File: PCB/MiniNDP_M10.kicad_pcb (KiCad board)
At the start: 2 copper layers, 72 x 26 mm, 22 parts, among them J1 Conn_02x20_Odd_Even, U1 AS6C8008_TSOPII, U2 HC238, U3 HC4040, U4 ABT841

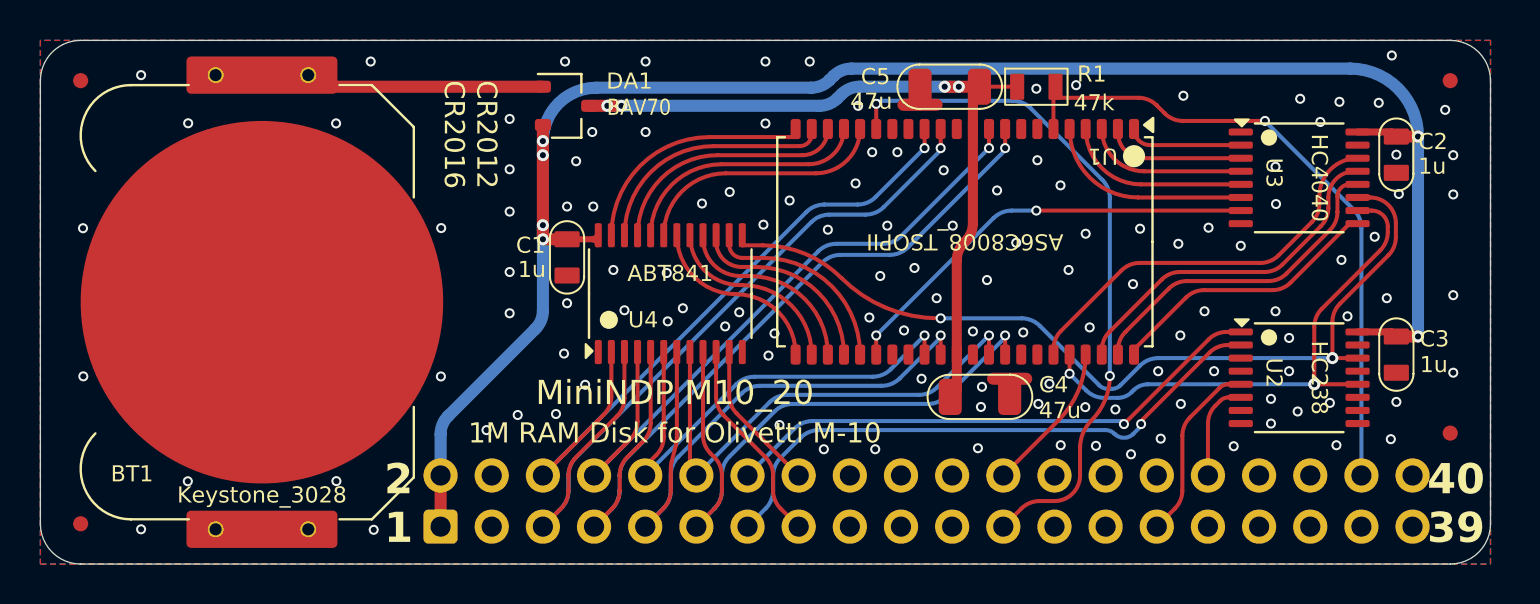
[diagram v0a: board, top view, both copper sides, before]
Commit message: M10 better layout, put old M10 versions in attic
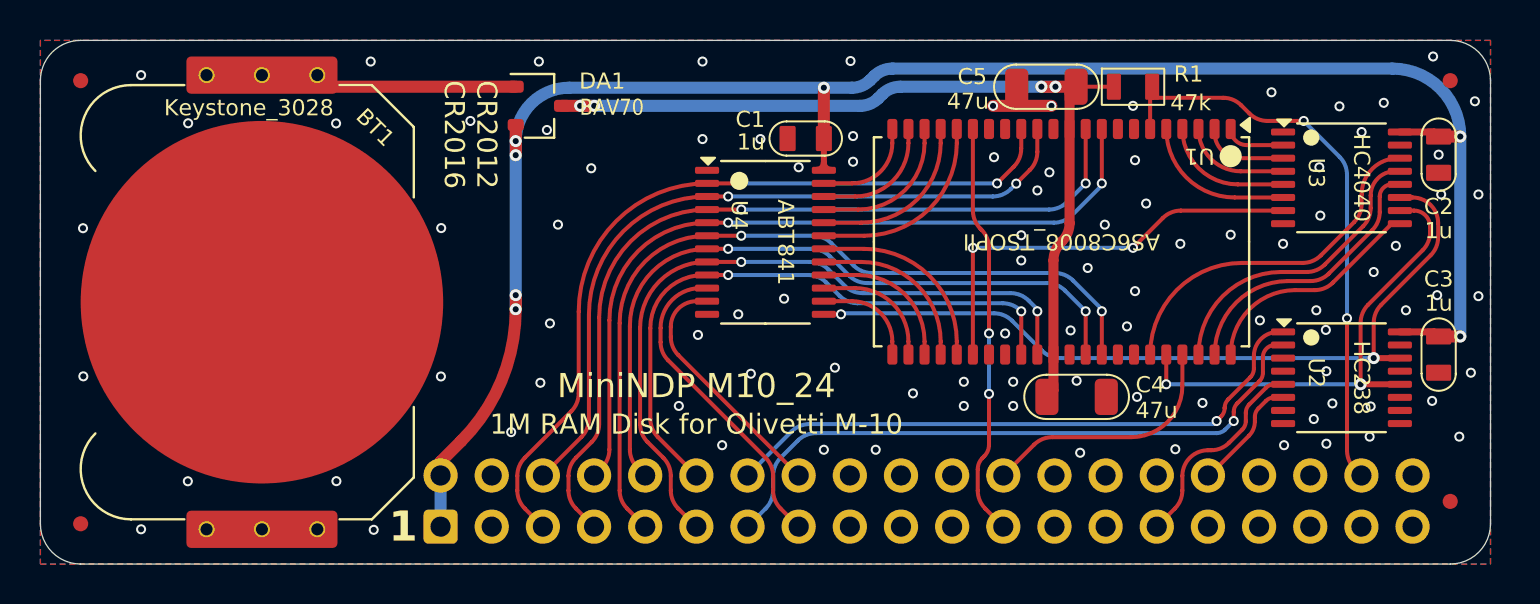
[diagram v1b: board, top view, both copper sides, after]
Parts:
- removed the REF** at (116.0, 116.3)
- removed the REF** at (120.7, 93.8)
- removed the REF** at (116.0, 93.8)
- removed the REF** at (120.7, 116.3)
- added REF**: pth_nail, 000_LOCAL:pth_nail, F.Cu at (118.3, 93.8)
- added REF**: pth_nail, 000_LOCAL:pth_nail, F.Cu at (121.1, 116.3)
- added REF**: pth_nail, 000_LOCAL:pth_nail, F.Cu at (118.3, 116.3)
- added REF**: pth_nail, 000_LOCAL:pth_nail, F.Cu at (115.6, 116.3)
- added REF**: pth_nail, 000_LOCAL:pth_nail, F.Cu at (121.1, 93.8)
- added REF**: pth_nail, 000_LOCAL:pth_nail, F.Cu at (115.6, 93.8)
- moved C1 13.2 mm to (145.3, 96.9), turned to 180 degrees
- moved U4 5.37 mm to (143.3, 102.0), turned to 0 degrees
- moved C4 4.80 mm to (158.8, 109.7)
- moved C5 4.80 mm to (157.3, 94.3)
- moved U1 4.80 mm to (158.1, 102.0)
- moved R1 4.80 mm to (161.6, 94.3)
- moved F3 3.39 mm to (177.3, 114.9)
- moved C2 2.10 mm to (176.8, 97.7)
- moved C3 2.10 mm to (176.8, 107.6)
- moved U2 2.10 mm to (172.0, 108.8)
- moved U3 2.10 mm to (171.9, 98.9)
- moved DA1 1.35 mm to (132.1, 95.3)
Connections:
- U1 pad 10: /AD2 -> /AD3
- U1 pad 13: /AD1 -> /AD0
- U1 pad 14: /AD0 -> /AD1
- U1 pad 23: /A15 -> /A19
- U1 pad 24: /A16 -> /A18
- U1 pad 26: /A18 -> /A16
- U1 pad 27: /A19 -> /A15
- U1 pad 31: /AD4 -> /AD6
- U1 pad 32: /AD5 -> /AD7
- U1 pad 35: /AD6 -> /AD4
- U1 pad 36: /AD7 -> /AD5
- U1 pad 9: /AD3 -> /AD2
- U4 pad 2: /AD0 -> /AD1
- U4 pad 3: /AD1 -> /AD0
- U4 pad 4: /AD2 -> /AD3
- U4 pad 5: /AD3 -> /AD2
- U4 pad 6: /AD4 -> /AD5
- U4 pad 7: /AD5 -> /AD4
- U4 pad 8: /AD6 -> /AD7
- U4 pad 9: /AD7 -> /AD6
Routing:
- net /~{WR}: track 34.2 -> 20.6 mm
- net /AD4: track 24.0 -> 35.6 mm, vias 1 -> 2
- net /AD5: track 29.6 -> 40.4 mm, vias 1 -> 2
- net /A10: track 12.1 -> 5.16 mm
- net /AD6: track 24.5 -> 30.7 mm, vias 1 -> 2
- net VMEM: track 38.8 -> 44.9 mm
- net /A11: track 12.2 -> 6.31 mm
- net /BUS_A11: track 10.2 -> 15.9 mm
- net /~{RD}: track 7.48 -> 12.5 mm
- net /BUS_A10: track 7.50 -> 12.4 mm
- net /AD7: track 30.5 -> 35.3 mm, vias 1 -> 2
- net /A12: track 12.3 -> 7.45 mm
- net /A19: track 9.87 -> 5.11 mm
- net /BLOCK: track 44.3 -> 39.9 mm
- net /AD2: track 34.1 -> 38.5 mm, vias 1 -> 2
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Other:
- board text added: "1"
- board text removed: "2 1"
- board text removed: "40 39"

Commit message: M10 trace optim
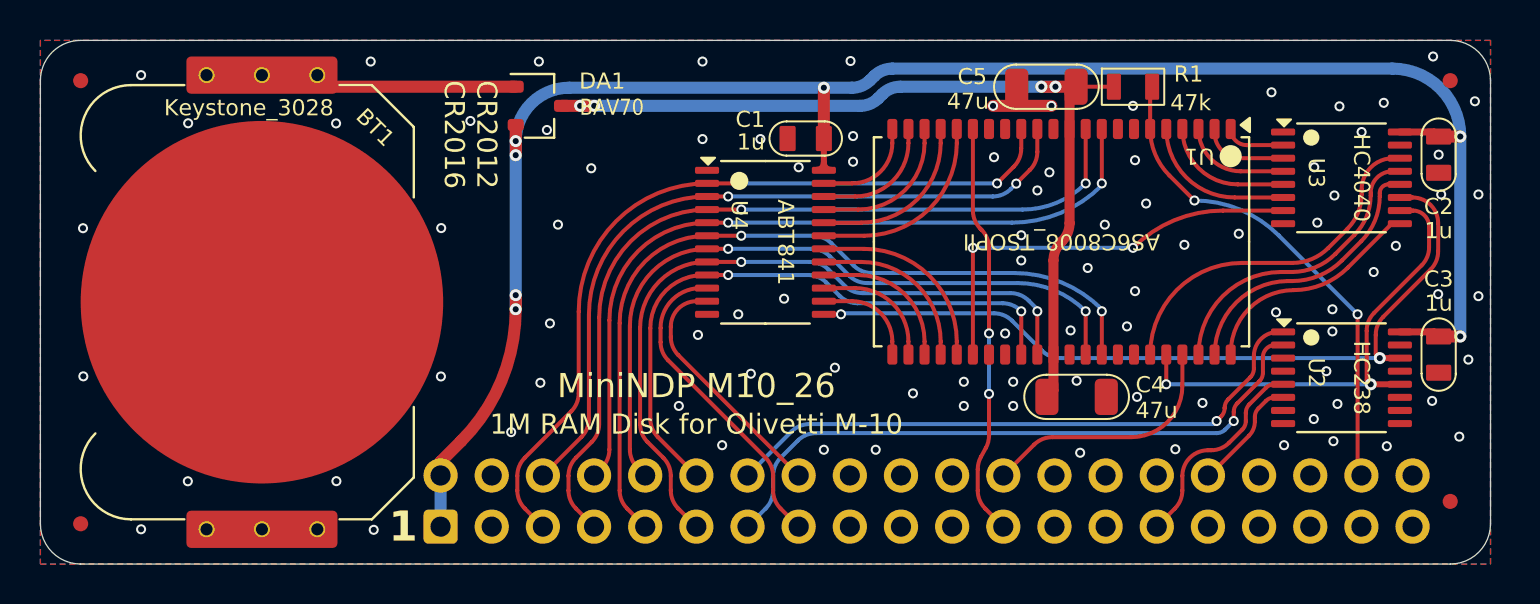
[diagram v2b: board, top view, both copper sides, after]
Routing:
- net /RAMRST: track 29.2 -> 24.7 mm
- net GND: vias 94 -> 92

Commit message: M10 via too close to u4p13
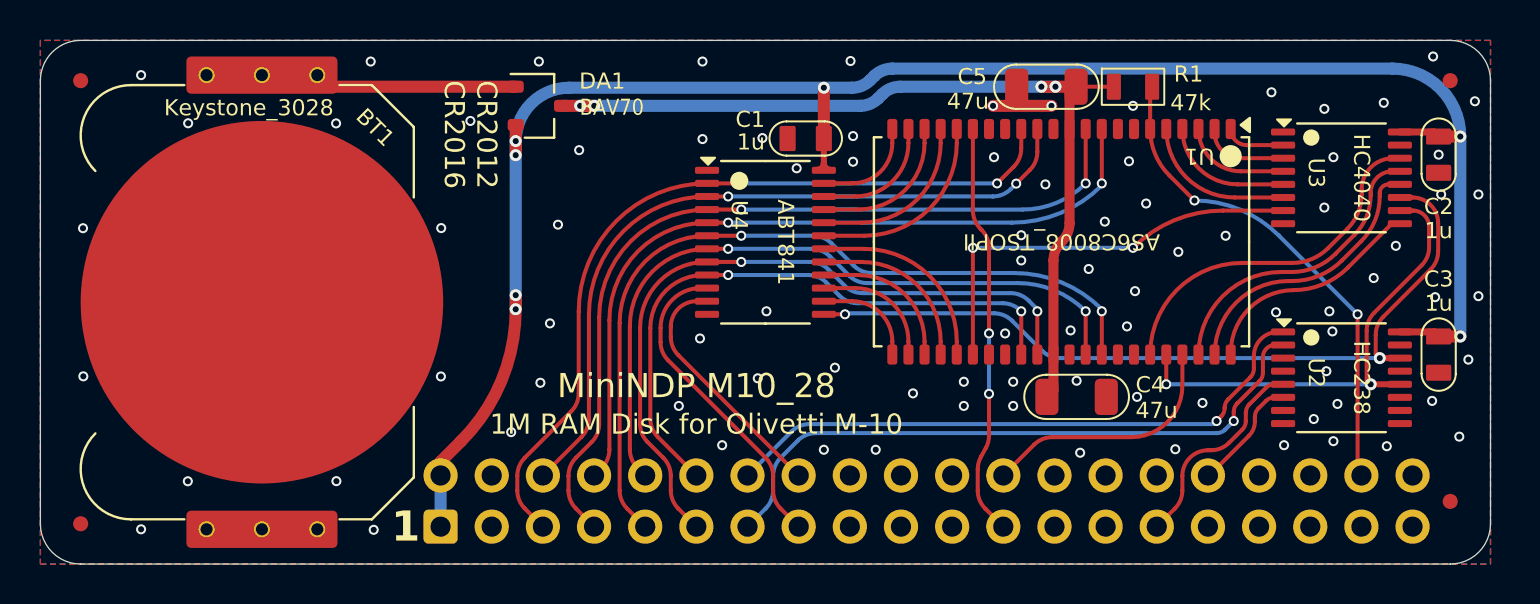
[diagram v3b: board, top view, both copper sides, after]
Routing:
- net GND: vias 92 -> 87

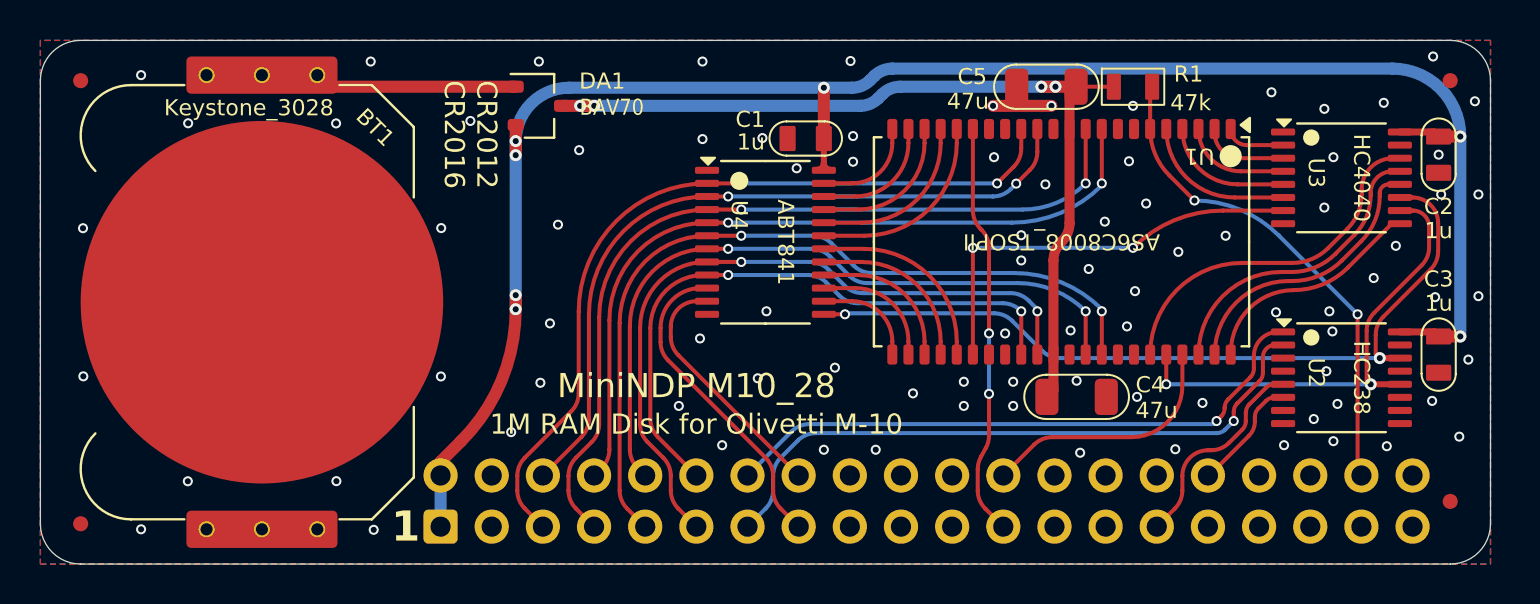
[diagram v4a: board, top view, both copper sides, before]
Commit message: M10 bus connector
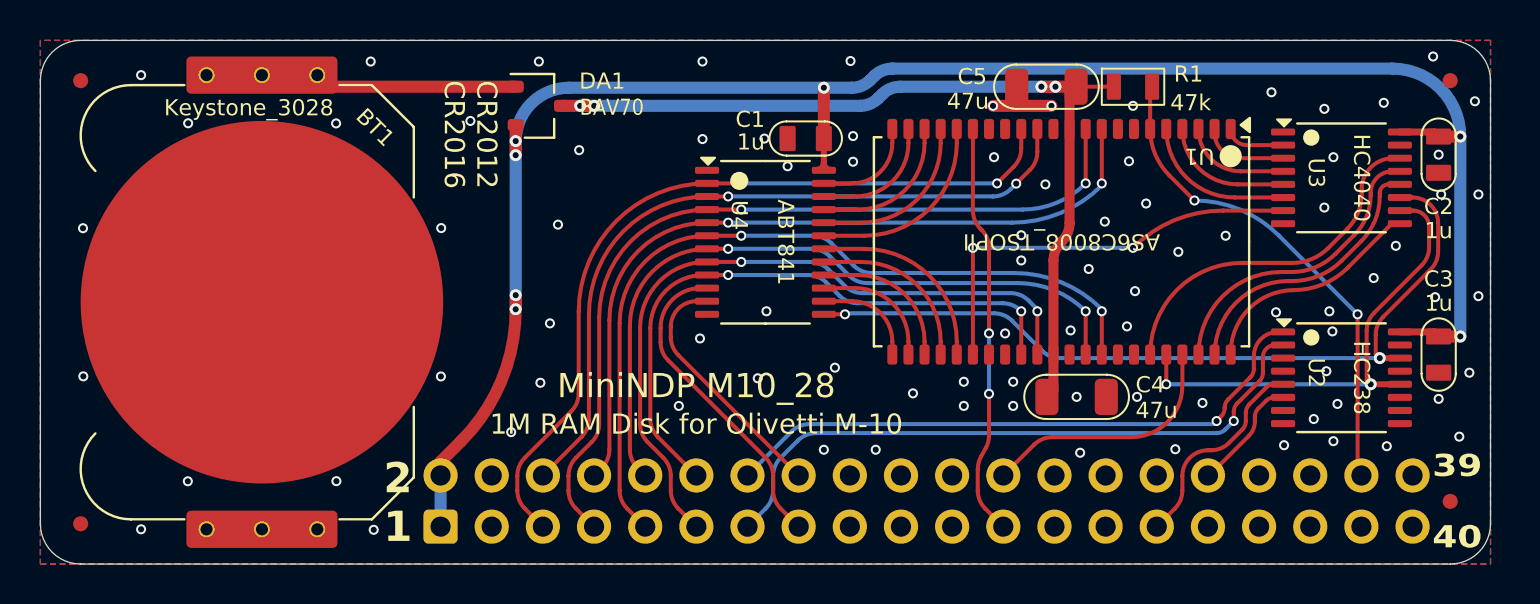
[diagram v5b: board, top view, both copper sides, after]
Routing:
- net GND: vias 87 -> 86
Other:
- board text added: "2 1"
- board text added: "39 40"
- board text removed: "1"

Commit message: M10 silkscreen typo bus pin numbers
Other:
- board text added: "40 39"
- board text removed: "39 40"
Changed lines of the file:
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@@
 		)
 	)
-	(gr_text "39\n\n40"
+	(gr_text "40\n\n39"
 		(at 177.7 114.915 0)
 		(layer "F.SilkS")

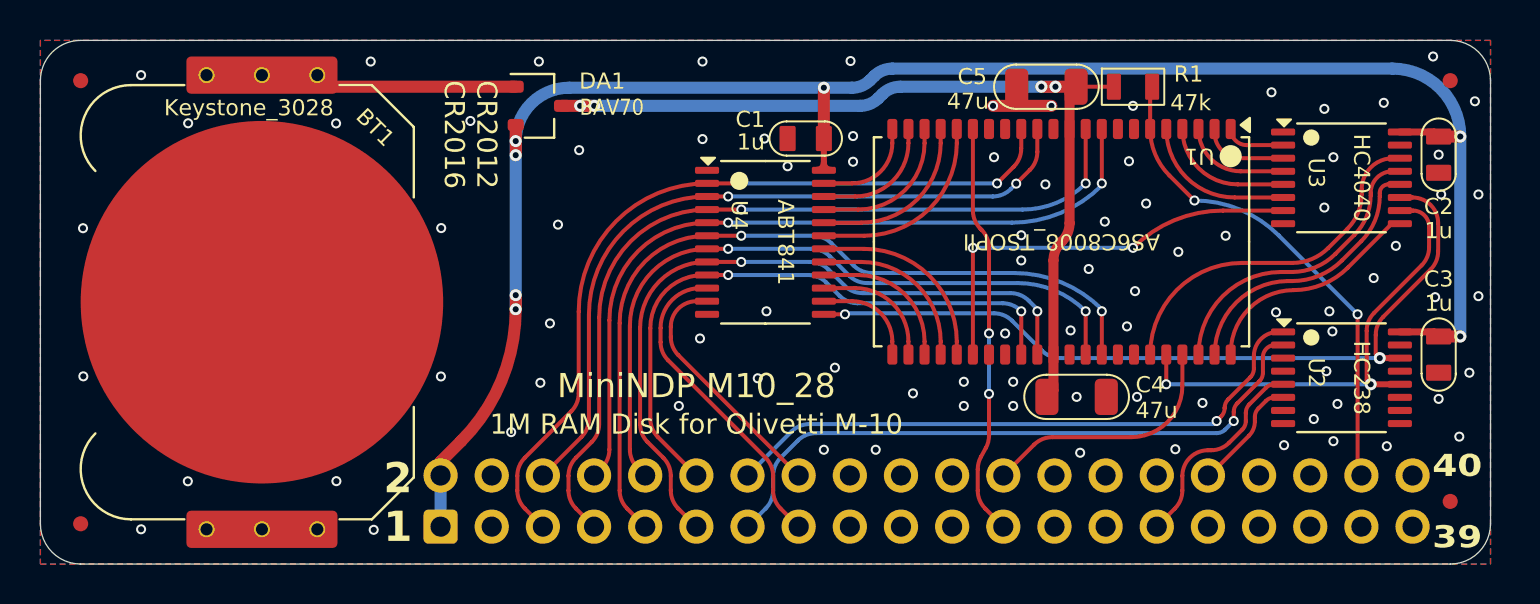
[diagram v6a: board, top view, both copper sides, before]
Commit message: M10 move chips a little
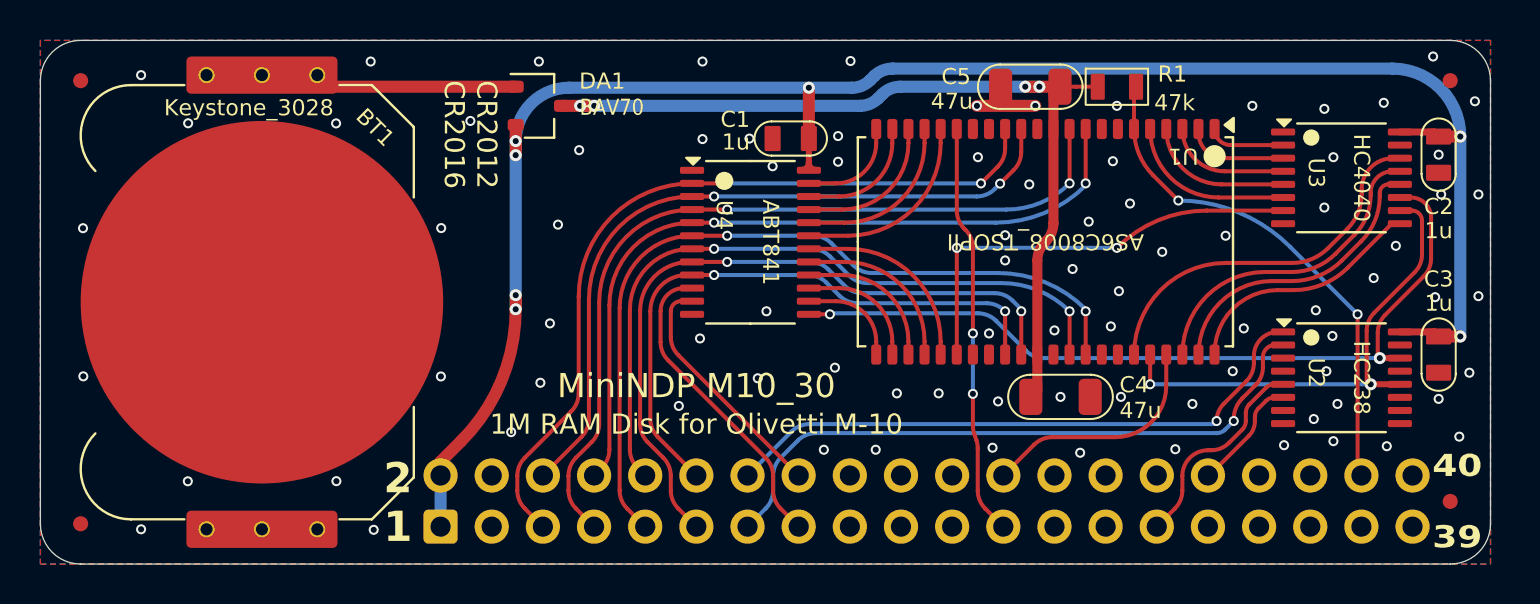
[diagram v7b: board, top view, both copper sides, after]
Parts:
- moved C4 0.80 mm to (158.0, 109.7)
- moved C5 0.80 mm to (156.5, 94.3)
- moved U1 0.80 mm to (157.2, 102.0)
- moved R1 0.80 mm to (160.8, 94.3)
- moved C1 0.74 mm to (144.6, 96.9)
- moved U4 0.74 mm to (142.6, 102.0)
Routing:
- net /A7: track 14.8 -> 15.6 mm
- net VMEM: track 44.9 -> 44.1 mm
- net /A4: track 4.25 -> 5.05 mm
- net /A3: track 6.46 -> 7.26 mm
- net /A1: track 21.2 -> 22.0 mm
- net /A2: track 7.60 -> 8.40 mm
- net /A5: track 3.02 -> 3.82 mm
- net /A9: track 17.6 -> 18.4 mm
- net /A8: track 13.7 -> 14.5 mm
- net /~{RD}: track 12.5 -> 11.7 mm
- net /A6: track 5.31 -> 6.11 mm
- net /A0: track 11.3 -> 12.1 mm
- net /RAMRST: track 24.7 -> 25.4 mm

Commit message: simplify covers, strengthen battery holders, silkscreen, readme
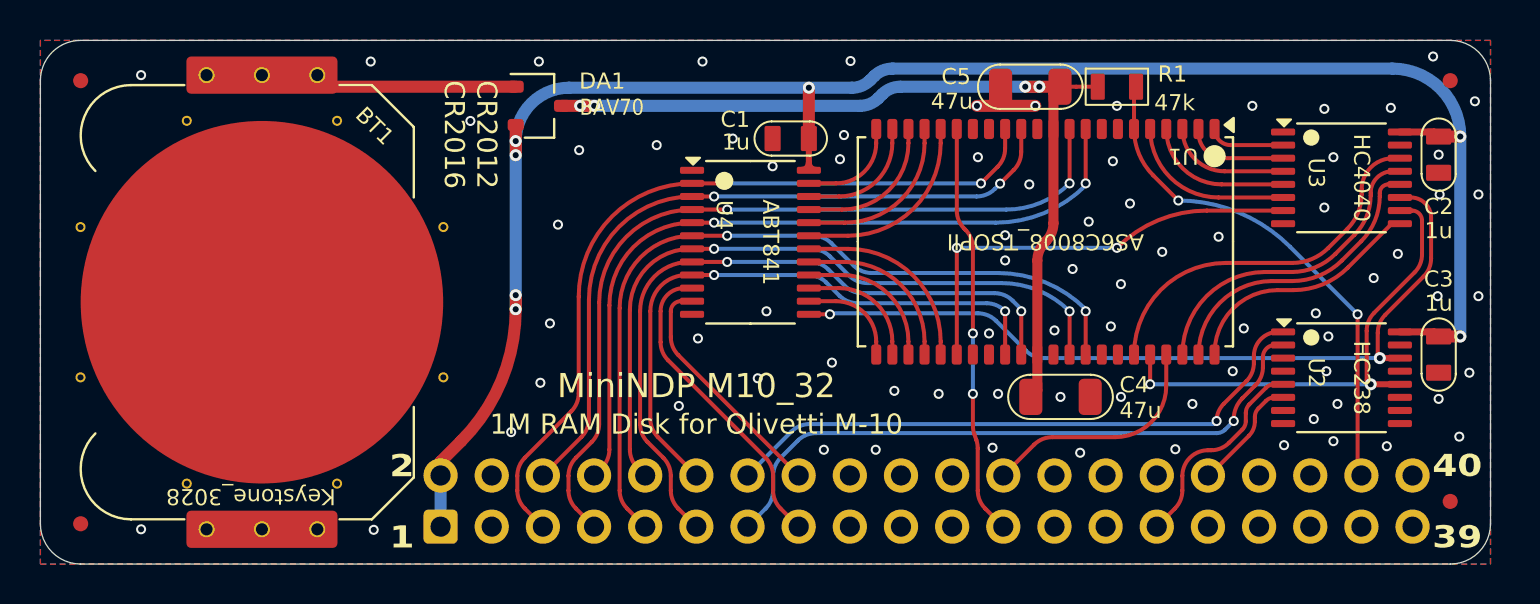
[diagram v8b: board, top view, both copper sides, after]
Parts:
- removed REF** (x6): pth_nail, 000_LOCAL:pth_nail
- BT1: footprint 000_LOCAL:Keystone_3028_3034 -> 000_LOCAL:Keystone_3028_3034_bkw
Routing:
- net GND: vias 86 -> 78
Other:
- board text added: "bank 0-3: P=129,133,137,141 block 0-255: OUT P,N read byte: D=INP(131) write byte: OUT 131,D"
- board text removed: "bank0-3: P=129,133,137,141 block0-255: OUT P,N read byte: N=INP(131) write byte: OUT 131,N"
